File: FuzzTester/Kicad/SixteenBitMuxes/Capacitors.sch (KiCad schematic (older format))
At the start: 10 parts, among them U4 CD4051B

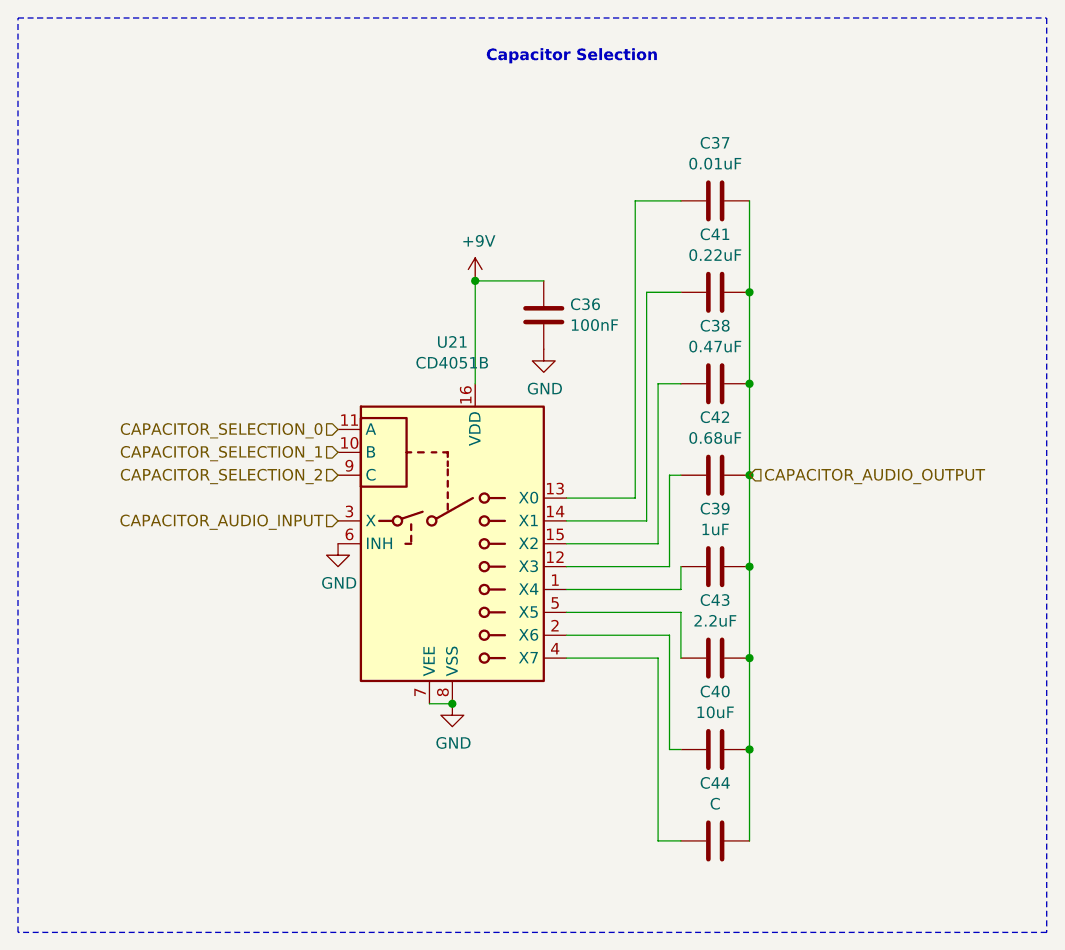
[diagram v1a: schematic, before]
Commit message: Finished (but not beautiful) PCB without SPI and most 8 channel multiplexers.
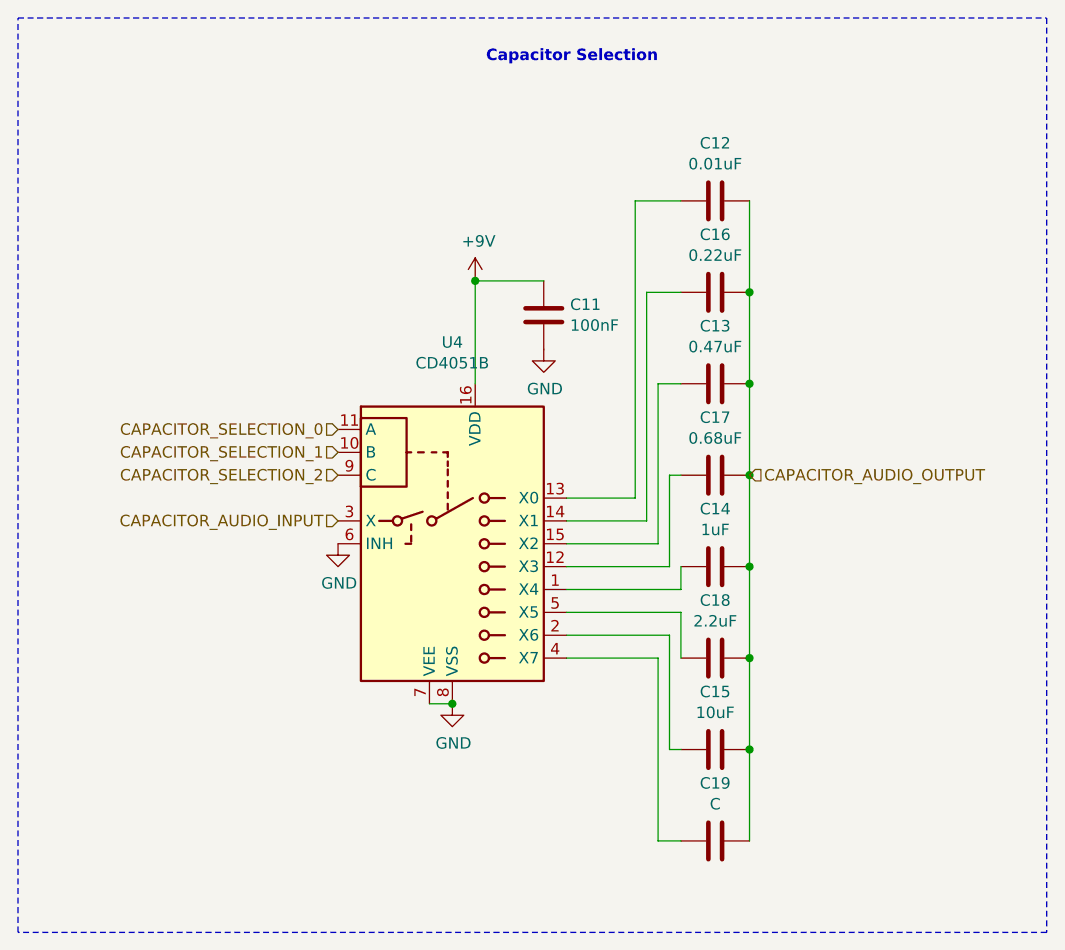
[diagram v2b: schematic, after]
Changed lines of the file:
@@
 AR Path="/5E983DF3/5E9AD572" Ref="C17"  Part="1"
 AR Path="/5F9F739D/5E9AD572" Ref="C42"  Part="1"
-F 0 "C42" V 5248 3450 50  0000 C CNN
+F 0 "C17" V 5248 3450 50  0000 C CNN
 F 1 "0.68uF" V 5339 3450 50  0000 C CNN
 F 2 "Capacitor_SMD:C_0805_2012Metric_Pad1.15x1.40mm_HandSolder" H 5538 3300 50  0001 C CNN
@@
 AR Path="/5E983DF3/5E9AD584" Ref="C16"  Part="1"
 AR Path="/5F9F739D/5E9AD584" Ref="C41"  Part="1"
-F 0 "C41" V 5248 2650 50  0000 C CNN
+F 0 "C16" V 5248 2650 50  0000 C CNN
 F 1 "0.22uF" V 5339 2650 50  0000 C CNN
 F 2 "Capacitor_SMD:C_0805_2012Metric_Pad1.15x1.40mm_HandSolder" H 5538 2500 50  0001 C CNN
@@
 AR Path="/5E983DF3/5E9AD58A" Ref="C14"  Part="1"
 AR Path="/5F9F739D/5E9AD58A" Ref="C39"  Part="1"
-F 0 "C39" V 5248 3850 50  0000 C CNN
+F 0 "C14" V 5248 3850 50  0000 C CNN
 F 1 "1uF" V 5339 3850 50  0000 C CNN
 F 2 "Capacitor_SMD:C_0805_2012Metric_Pad1.15x1.40mm_HandSolder" H 5538 3700 50  0001 C CNN
@@
 AR Path="/5E983DF3/5E9AD596" Ref="C13"  Part="1"
 AR Path="/5F9F739D/5E9AD596" Ref="C38"  Part="1"
-F 0 "C38" V 5248 3050 50  0000 C CNN
+F 0 "C13" V 5248 3050 50  0000 C CNN
 F 1 "0.47uF" V 5339 3050 50  0000 C CNN
 F 2 "Capacitor_SMD:C_0805_2012Metric_Pad1.15x1.40mm_HandSolder" H 5538 2900 50  0001 C CNN
@@
 AR Path="/5E983DF3/5E9AD59F" Ref="C11"  Part="1"
 AR Path="/5F9F739D/5E9AD59F" Ref="C36"  Part="1"
-F 0 "C36" H 4865 2796 50  0000 L CNN
+F 0 "C11" H 4865 2796 50  0000 L CNN
 F 1 "100nF" H 4865 2705 50  0000 L CNN
 F 2 "Capacitor_SMD:C_0805_2012Metric_Pad1.15x1.40mm_HandSolder" H 4788 2600 50  0001 C CNN
@@
 AR Path="/5E983DF3/5E9AD590" Ref="C12"  Part="1"
 AR Path="/5F9F739D/5E9AD590" Ref="C37"  Part="1"
-F 0 "C37" V 5248 2250 50  0000 C CNN
+F 0 "C12" V 5248 2250 50  0000 C CNN
 F 1 "0.01uF" V 5339 2250 50  0000 C CNN
 F 2 "Capacitor_SMD:C_0805_2012Metric_Pad1.15x1.40mm_HandSolder" H 5538 2100 50  0001 C CNN
@@
 AR Path="/5E983DF3/5E9AD57E" Ref="C15"  Part="1"
 AR Path="/5F9F739D/5E9AD57E" Ref="C40"  Part="1"
-F 0 "C40" V 5248 4650 50  0000 C CNN
+F 0 "C15" V 5248 4650 50  0000 C CNN
 F 1 "10uF" V 5339 4650 50  0000 C CNN
 F 2 "Capacitor_SMD:C_0805_2012Metric_Pad1.15x1.40mm_HandSolder" H 5538 4500 50  0001 C CNN
@@
 AR Path="/5E983DF3/5E9AD5F3" Ref="C19"  Part="1"
 AR Path="/5F9F739D/5E9AD5F3" Ref="C44"  Part="1"
-F 0 "C44" V 5248 5050 50  0000 C CNN
+F 0 "C19" V 5248 5050 50  0000 C CNN
 F 1 "C" V 5339 5050 50  0000 C CNN
 F 2 "Capacitor_SMD:C_0805_2012Metric_Pad1.15x1.40mm_HandSolder" H 5538 4900 50  0001 C CNN
@@
 AR Path="/5E983DF3/5E9AD578" Ref="C18"  Part="1"
 AR Path="/5F9F739D/5E9AD578" Ref="C43"  Part="1"
-F 0 "C43" V 5248 4250 50  0000 C CNN
+F 0 "C18" V 5248 4250 50  0000 C CNN
 F 1 "2.2uF" V 5339 4250 50  0000 C CNN
 F 2 "Capacitor_SMD:C_0805_2012Metric_Pad1.15x1.40mm_HandSolder" H 5538 4100 50  0001 C CNN
@@
 AR Path="/5E983DF3/5E9AD56C" Ref="U4"  Part="1"
 AR Path="/5F9F739D/5E9AD56C" Ref="U21"  Part="1"
-F 0 "U21" H 4350 4631 50  0000 C CNN
+F 0 "U4" H 4350 4631 50  0000 C CNN
 F 1 "CD4051B" H 4350 4540 50  0000 C CNN
 F 2 "Package_SO:SOIC-16_3.9x9.9mm_P1.27mm" H 4500 3000 50  0001 L CNN
